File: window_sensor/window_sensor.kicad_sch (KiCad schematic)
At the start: 22 parts, among them J1 UART, J2 SWD, J3 Screw_Terminal_01x02, U1 RFM69HW, U2 STM32G031K8Tx, U3 PAM2401, Y1 32.768KHz

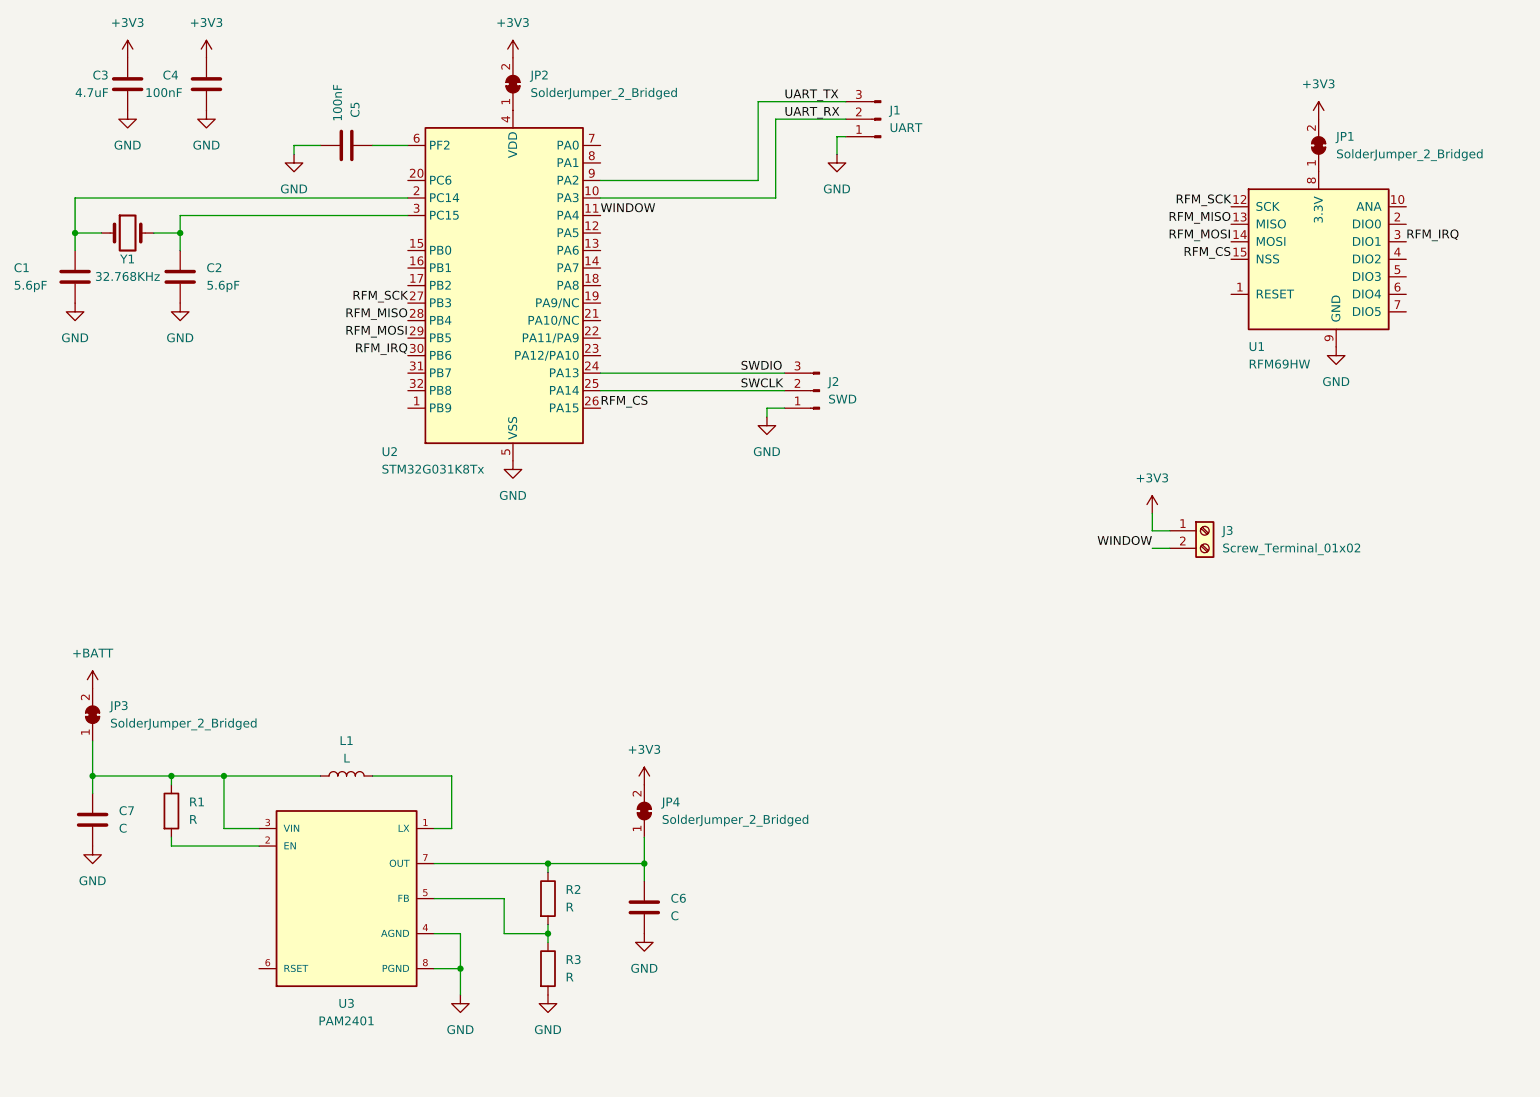
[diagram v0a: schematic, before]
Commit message: removed step-up, using direct VBAT
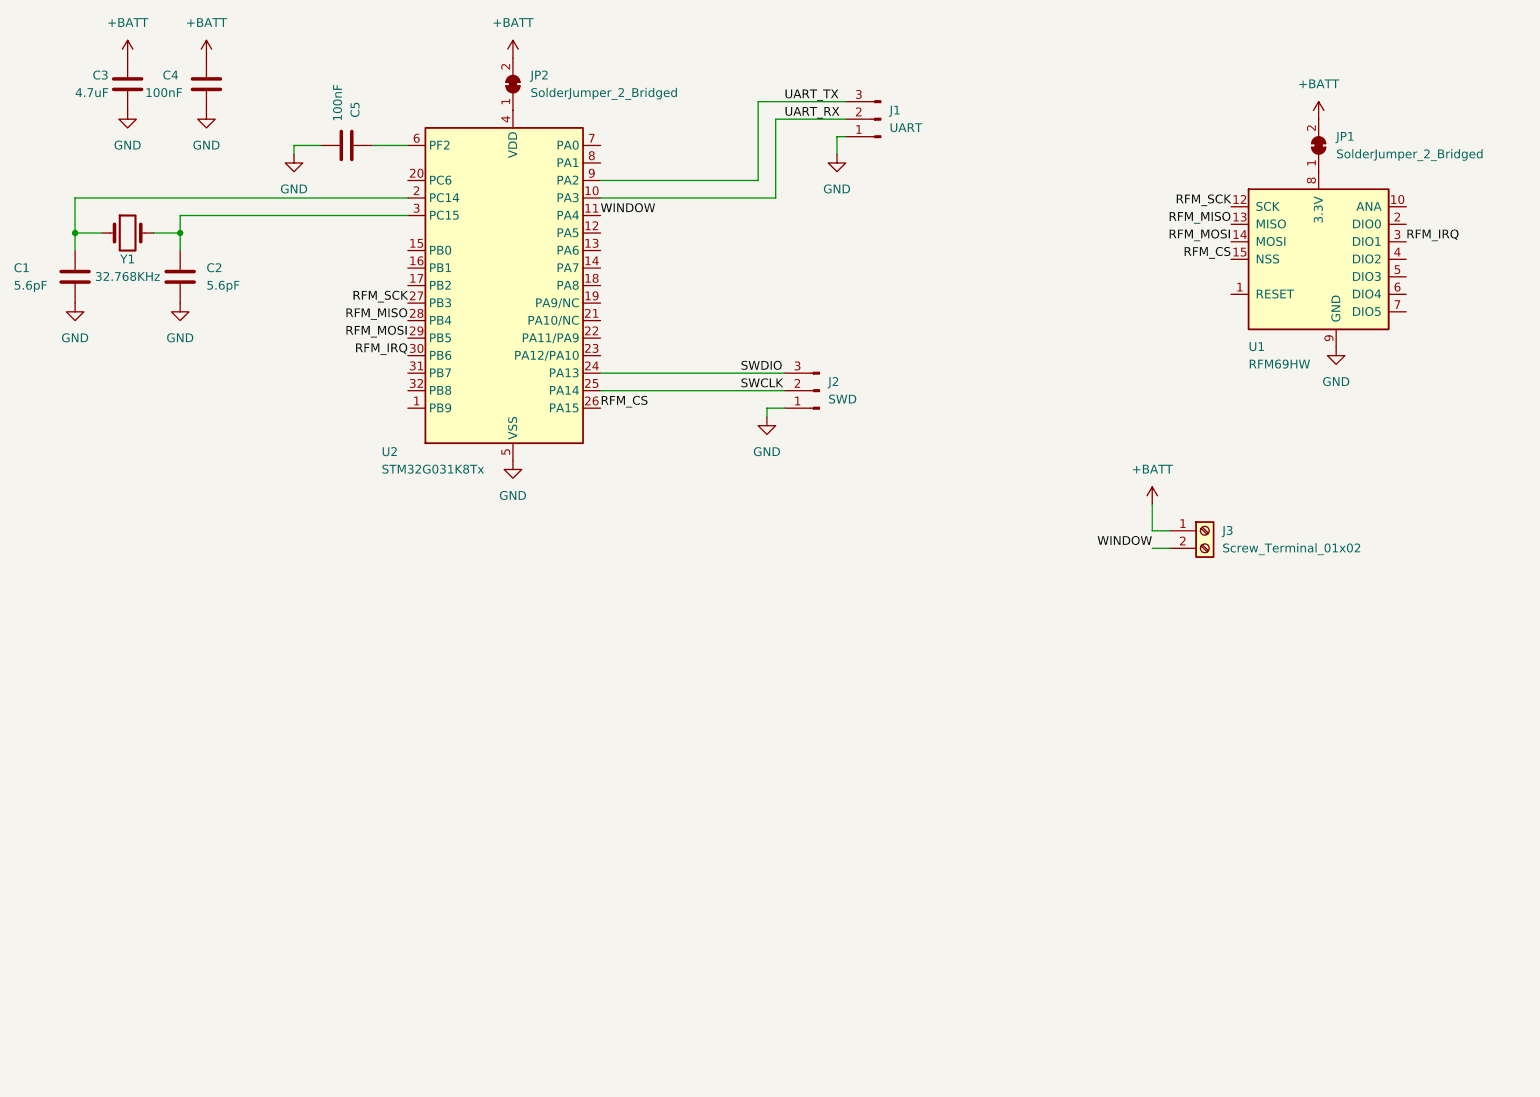
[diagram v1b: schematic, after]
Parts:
- removed C6, C7: C, symbol Device:C
- removed JP3, JP4: SolderJumper_2_Bridged, symbol Jumper:SolderJumper_2_Bridged
- removed L1: L, symbol Device:L
- removed R1, R2, R3: R, symbol Device:R
- removed U3: PAM2401, PAM2401:MSOP8, symbol sensor:PAM2401
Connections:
- net +3V3 is gone; now on net +BATT: C3.1, C4.1, J3.1 (Pin_1), JP1.2 (B), JP2.2 (B)

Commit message: debugging connectors unified to one
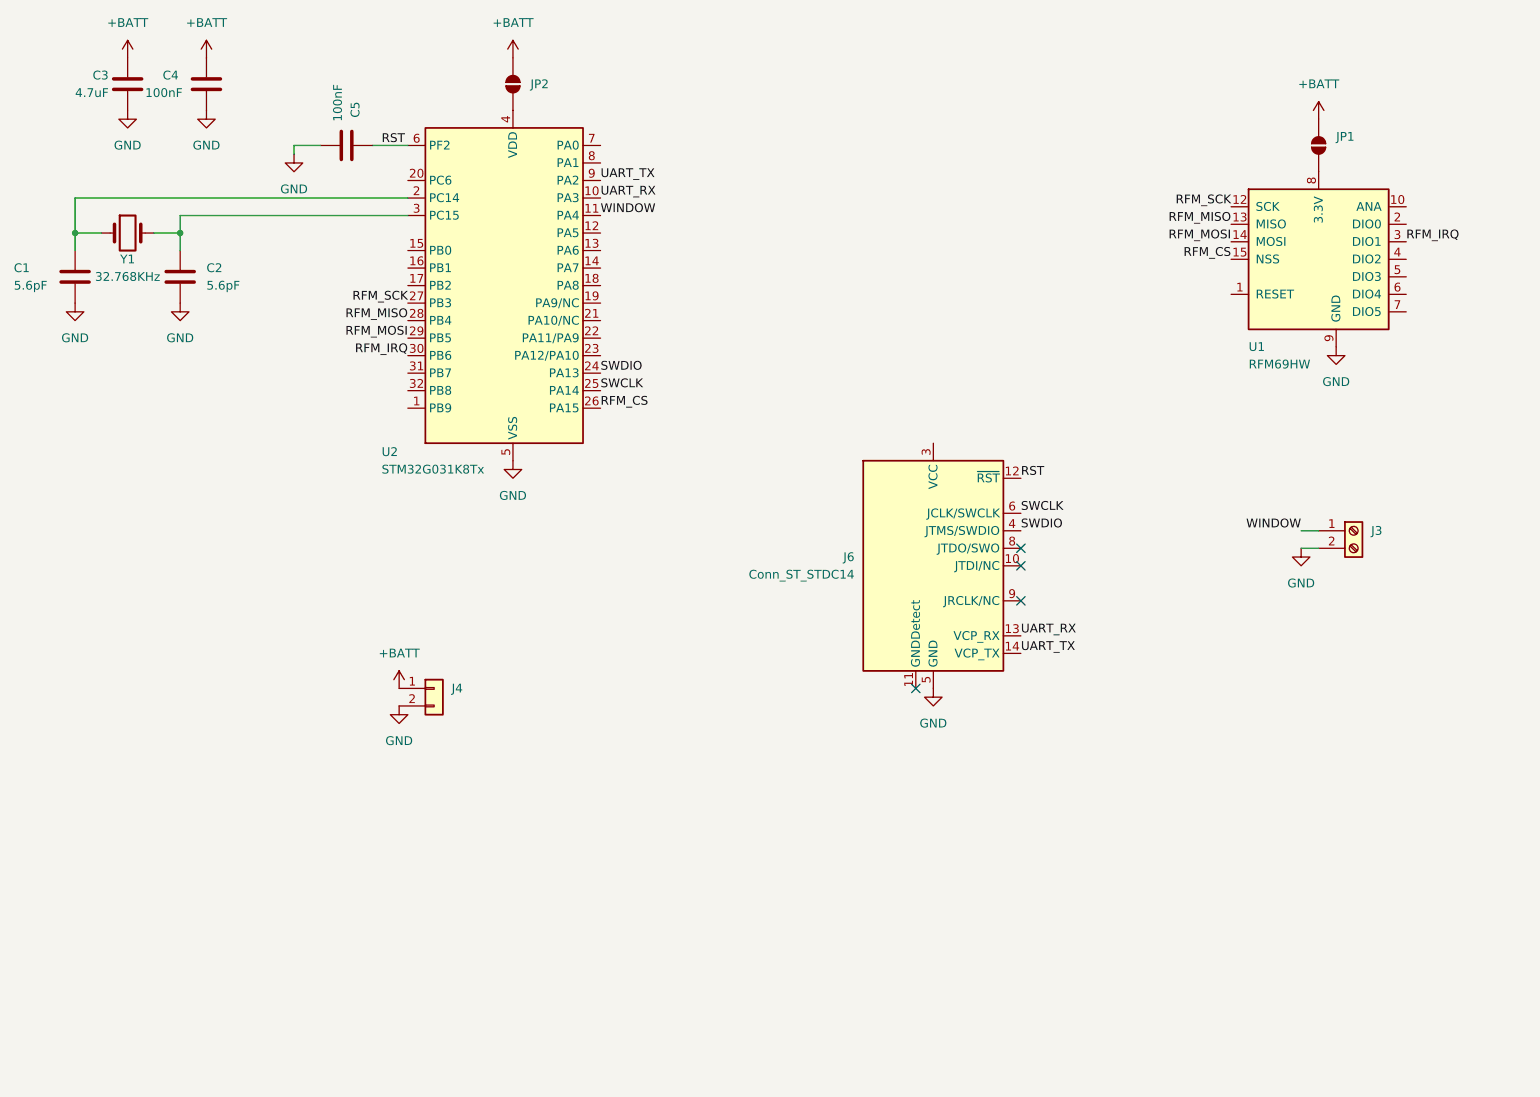
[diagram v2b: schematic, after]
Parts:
- removed J1: UART, symbol Connector:Conn_01x03_Pin
- removed J2: SWD, symbol Connector:Conn_01x03_Pin
- added J4: Conn_01x02, Connector_PinHeader_2.54mm:PinHeader_1x02_P2.54mm_Vertical, symbol Connector_Generic:Conn_01x02
- added J6: Conn_ST_STDC14, Connector_PinHeader_1.27mm:PinHeader_2x07_P1.27mm_Vertical_SMD, symbol Connector:Conn_ST_STDC14
- C1, C2, C3, C4, C5: footprint (none) -> Capacitor_SMD:C_0805_2012Metric_Pad1.18x1.45mm_HandSolder
- J3: footprint (none) -> TerminalBlock:TerminalBlock_Xinya_XY308-2.54-2P_1x02_P2.54mm_Horizontal
- JP1, JP2: footprint (none) -> Jumper:SolderJumper-2_P1.3mm_Open_TrianglePad1.0x1.5mm; symbol Jumper:SolderJumper_2_Bridged -> Jumper:SolderJumper_2_Open; now left out of the parts list
- Y1: footprint (none) -> Crystal:Crystal_SMD_3215-2Pin_3.2x1.5mm; manf# (none) -> MPJK-7L-32.768-12.5-20-70-C
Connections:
- net +BATT: now also J4.1 (Pin_1); no longer J3.1 (Pin_1)
- net GND: now also J3.2 (Pin_2), J4.2 (Pin_2), J6.5 (GND), J6.7 (GND)
- net SWCLK: now also J6.6 (JCLK/SWCLK)
- net SWDIO: now also J6.4 (JTMS/SWDIO)
- net UART_RX: now also J6.13 (VCP_RX)
- net UART_TX: now also J6.14 (VCP_TX)
- net WINDOW: now also J3.1 (Pin_1); no longer J3.2 (Pin_2)
- net RST: now reaches C5.1, U2.6 (PF2)
- net RST: now also J6.12 (~{RST})
- no-connect marks 0 -> 4
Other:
- moved on the sheet: J3

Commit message: moved wakeup to PA0
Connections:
- net WINDOW: now also U2.7 (PA0); no longer U2.11 (PA4)
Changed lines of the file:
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@@
-		)
-	)
-	(label "WINDOW"
-		(at 113.03 43.18 0)
-		(fields_autoplaced yes)
-		(effects
-			(font
-				(size 1.27 1.27)
-			)
-			(justify left bottom)
 		)
 	)
@@
 		)
 	)
+	(label "WINDOW"
+		(at 113.03 33.02 0)
+		(fields_autoplaced yes)
+		(effects
+			(font
+				(size 1.27 1.27)
+			)
+			(justify left bottom)
+		)
+	)
